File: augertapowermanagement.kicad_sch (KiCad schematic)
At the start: 27 parts, among them J1 Screw_Terminal_01x02, J10 Screw_Terminal_01x10, J11 Screw_Terminal_01x10, J12 gnd block, J2 76825-0002, J3 USB_A_Stacked, J4 USB_A_Stacked, J5 USB_A_Stacked, J6 USB_A_Stacked, J7 Screw_Terminal_01x08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

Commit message: update
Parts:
- removed Q1: IRF6623, Package_DirectFET:DirectFET_ST, symbol Transistor_FET:IRF6623
- added K2: J107F1CS203VDC.80, cit:Relay_J107F, symbol Relay:DIPxx-1Cxx-51x
- added R16: 10k, Resistor_SMD:R_1210_3225Metric_Pad1.30x2.65mm_HandSolder, symbol Device:R_US
- TP1, TP3, TP4, TP5: Purchase (none) -> JUST PAD
- U24: Purchase (none) -> IN LAB
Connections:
- net +BATT: now also K2.7
- net -BATT: now also R2.1, K2.6, R16.2; no longer SW1.3 (C)
- net at C2.1, J9.1 (Pin_1), J9.2 (Pin_2)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: now also SW1.2 (B), TP3.1; no longer R2.1
- net at JP1.1 (A), JP5.2 (B), K1.7: now also K2.14; no longer K1.8
- new net: K2.1, R16.1
- new net: K2.2, SW1.1 (A)
- new net: R2.2, SW1.3 (C)
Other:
- moved on the sheet: R2, SW1, TP3

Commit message: update
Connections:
- net at J11.1 (Pin_1): now also U2.38 (CLK); no longer U2.36 (SD1)
- net at J11.3 (Pin_3): now also U2.36 (SD1); no longer U2.38 (CLK)
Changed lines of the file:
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@@
+    (stroke (width 0) (type default) (color 0 0 0 0))
+  )
+  (wire (pts (xy 90.17 143.51) (xy 90.17 162.56))
     (stroke (width 0) (type default) (color 0 0 0 0))
   )
@@
     (stroke (width 0) (type default) (color 0 0 0 0))
   )
-  (wire (pts (xy 87.63 142.24) (xy 118.11 142.24))
-    (stroke (width 0) (type default) (color 0 0 0 0))
-  )
   (wire (pts (xy 76.2 71.12) (xy 113.03 71.12))
     (stroke (width 0) (type default) (color 0 0 0 0))
@@
     (stroke (width 0) (type default) (color 0 0 0 0))
   )
+  (wire (pts (xy 123.19 144.78) (xy 87.63 144.78))
+    (stroke (width 0) (type default) (color 0 0 0 0))
+  )
   (wire (pts (xy 118.11 92.71) (xy 121.92 92.71))
     (stroke (width 0) (type default) (color 0 0 0 0))
@@
     (stroke (width 0) (type default) (color 0 0 0 0))
   )
-  (wire (pts (xy 90.17 162.56) (xy 90.17 143.51))
-    (stroke (width 0) (type default) (color 0 0 0 0))
-  )
   (wire (pts (xy 72.39 162.56) (xy 72.39 118.11))
     (stroke (width 0) (type default) (color 0 0 0 0))
@@
     (stroke (width 0) (type default) (color 0 0 0 0))
   )
-  (wire (pts (xy 92.71 144.78) (xy 123.19 144.78))
-    (stroke (width 0) (type default) (color 0 0 0 0))
-  )
   (wire (pts (xy 177.8 106.68) (xy 176.53 106.68))
     (stroke (width 0) (type default) (color 0 0 0 0))
@@
     (stroke (width 0) (type default) (color 0 0 0 0))
   )
+  (wire (pts (xy 92.71 142.24) (xy 118.11 142.24))
+    (stroke (width 0) (type default) (color 0 0 0 0))
+  )
   (wire (pts (xy 248.92 50.8) (xy 251.46 50.8))
     (stroke (width 0) (type default) (color 0 0 0 0))
@@
     (stroke (width 0) (type default) (color 0 0 0 0))
   )
+  (wire (pts (xy 87.63 144.78) (xy 87.63 162.56))
+    (stroke (width 0) (type default) (color 0 0 0 0))
+  )
   (wire (pts (xy 77.47 130.81) (xy 40.64 130.81))
     (stroke (width 0) (type default) (color 0 0 0 0))
@@
     (stroke (width 0) (type default) (color 0 0 0 0))
   )
+  (wire (pts (xy 92.71 142.24) (xy 92.71 162.56))
+    (stroke (width 0) (type default) (color 0 0 0 0))
+  )
   (wire (pts (xy 201.93 96.52) (xy 266.7 96.52))
     (stroke (width 0) (type default) (color 0 0 0 0))
@@
     (stroke (width 0) (type default) (color 0 0 0 0))
   )
-  (wire (pts (xy 87.63 162.56) (xy 87.63 142.24))
-    (stroke (width 0) (type default) (color 0 0 0 0))
-  )
   (wire (pts (xy 180.34 50.8) (xy 180.34 45.72))
     (stroke (width 0) (type default) (color 0 0 0 0))
@@
     (stroke (width 0) (type default) (color 0 0 0 0))
   )
-  (wire (pts (xy 92.71 162.56) (xy 92.71 144.78))
-    (stroke (width 0) (type default) (color 0 0 0 0))
-  )

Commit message: update
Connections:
- net power_conversion/routerp: now also J7.1 (Pin_1)
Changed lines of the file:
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@@
   (junction (at 113.03 71.12) (diameter 0) (color 0 0 0 0)
   )
-  (junction (at 199.39 99.06) (diameter 0) (color 0 0 0 0)
+  (junction (at 175.26 93.98) (diameter 0) (color 0 0 0 0)
   )
   (junction (at 31.75 179.07) (diameter 0) (color 0 0 0 0)
@@
   (no_connect (at 190.5 144.78))
   (no_connect (at 190.5 147.32))
+  (wire (pts (xy 175.26 93.98) (xy 175.26 88.9))
+    (stroke (width 0) (type default) (color 0 0 0 0))
+  )
   (wire (pts (xy 118.11 107.95) (xy 139.7 107.95))
     (stroke (width 0) (type default) (color 0 0 0 0))
@@
     (stroke (width 0) (type default) (color 0 0 0 0))
   )
+  (wire (pts (xy 175.26 93.98) (xy 177.8 93.98))
+    (stroke (width 0) (type default) (color 0 0 0 0))
+  )
   (wire (pts (xy 199.39 55.88) (xy 199.39 58.42))
     (stroke (width 0) (type default) (color 0 0 0 0))
@@
     (stroke (width 0) (type default) (color 0 0 0 0))
   )
-  (wire (pts (xy 184.15 80.01) (xy 199.39 80.01))
+  (wire (pts (xy 184.15 81.28) (xy 199.39 81.28))
     (stroke (width 0) (type default) (color 0 0 0 0))
   )
@@
     (stroke (width 0) (type default) (color 0 0 0 0))
   )
-  (wire (pts (xy 187.96 127) (xy 187.96 82.55))
-    (stroke (width 0) (type default) (color 0 0 0 0))
-  )
   (wire (pts (xy 69.85 123.19) (xy 77.47 123.19))
     (stroke (width 0) (type default) (color 0 0 0 0))
@@
     (stroke (width 0) (type default) (color 0 0 0 0))
   )
+  (wire (pts (xy 187.96 82.55) (xy 187.96 127))
+    (stroke (width 0) (type default) (color 0 0 0 0))
+  )
   (wire (pts (xy 43.18 144.78) (xy 43.18 133.35))
     (stroke (width 0) (type default) (color 0 0 0 0))
@@
     (stroke (width 0) (type default) (color 0 0 0 0))
   )
+  (wire (pts (xy 199.39 81.28) (xy 199.39 99.06))
+    (stroke (width 0) (type default) (color 0 0 0 0))
+  )
   (wire (pts (xy 173.99 86.36) (xy 173.99 104.14))
     (stroke (width 0) (type default) (color 0 0 0 0))
@@
     (stroke (width 0) (type default) (color 0 0 0 0))
   )
-  (wire (pts (xy 146.05 93.98) (xy 177.8 93.98))
+  (wire (pts (xy 146.05 93.98) (xy 175.26 93.98))
     (stroke (width 0) (type default) (color 0 0 0 0))
   )
@@
     (stroke (width 0) (type default) (color 0 0 0 0))
   )
-  (wire (pts (xy 195.58 99.06) (xy 199.39 99.06))
+  (wire (pts (xy 175.26 88.9) (xy 177.8 88.9))
     (stroke (width 0) (type default) (color 0 0 0 0))
   )
@@
     (stroke (width 0) (type default) (color 0 0 0 0))
   )
+  (wire (pts (xy 184.15 80.01) (xy 184.15 81.28))
+    (stroke (width 0) (type default) (color 0 0 0 0))
+  )
   (wire (pts (xy 201.93 96.52) (xy 266.7 96.52))
     (stroke (width 0) (type default) (color 0 0 0 0))
@@
     (stroke (width 0) (type default) (color 0 0 0 0))
   )
-  (wire (pts (xy 199.39 80.01) (xy 199.39 99.06))
-    (stroke (width 0) (type default) (color 0 0 0 0))
-  )

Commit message: update
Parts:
- JP1, JP5: footprint Connector_PinHeader_2.00mm:PinHeader_1x02_P2.00mm_Horizontal -> cit:JUMPER_5102TR; Purchase NA, JUST pads -> https://www.digikey.com/en/products/detail/keystone-electro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
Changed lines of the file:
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@@
     (property "Reference" "JP1" (id 0) (at 100.33 29.21 0))
     (property "Value" "Jumper_2_Open" (id 1) (at 100.33 31.75 0))
-    (property "Footprint" "Connector_PinHeader_2.00mm:PinHeader_1x02_P2.00mm_Horizontal" (id 2) (at 100.33 35.56 0)
-      (effects (font (size 1.27 1.27)) hide)
-    )
-    (property "Datasheet" "~" (id 3) (at 100.33 35.56 0)
-      (effects (font (size 1.27 1.27)) hide)
-    )
-    (property "Purchase" "NA, JUST pads" (id 4) (at 100.33 35.56 0)
+    (property "Footprint" "cit:JUMPER_5102TR" (id 2) (at 100.33 35.56 0)
+      (effects (font (size 1.27 1.27)) hide)
+    )
+    (property "Datasheet" "https://www.digikey.com/en/products/detail/keystone-electronics/5102TR/4759688" (id 3) (at 100.33 35.56 0)
+      (effects (font (size 1.27 1.27)) hide)
+    )
+    (property "Purchase" "https://www.digikey.com/en/products/detail/keystone-electronics/5102TR/4759688" (id 4) (at 100.33 35.56 0)
       (effects (font (size 1.27 1.27)) hide)
     )
@@
     (property "Reference" "JP5" (id 0) (at 50.8 34.29 0))
     (property "Value" "Jumper_2_Open" (id 1) (at 60.96 36.83 0))
-    (property "Footprint" "Connector_PinHeader_2.00mm:PinHeader_1x02_P2.00mm_Horizontal" (id 2) (at 50.8 40.64 0)
-      (effects (font (size 1.27 1.27)) hide)
-    )
-    (property "Datasheet" "~" (id 3) (at 50.8 40.64 0)
-      (effects (font (size 1.27 1.27)) hide)
-    )
-    (property "Purchase" "NA, JUST pads" (id 4) (at 50.8 40.64 0)
+    (property "Footprint" "cit:JUMPER_5102TR" (id 2) (at 50.8 40.64 0)
+      (effects (font (size 1.27 1.27)) hide)
+    )
+    (property "Datasheet" "https://www.digikey.com/en/products/detail/keystone-electronics/5102TR/4759688" (id 3) (at 50.8 40.64 0)
+      (effects (font (size 1.27 1.27)) hide)
+    )
+    (property "Purchase" "https://www.digikey.com/en/products/detail/keystone-electronics/5102TR/4759688" (id 4) (at 50.8 40.64 0)
       (effects (font (size 1.27 1.27)) hide)
     )
@@
     )
     (path "/74a29476-3c13-4143-84d6-566dfae4024a"
-      (reference "JP1") (unit 1) (value "Jumper_2_Open") (footprint "Connector_PinHeader_2.00mm:PinHeader_1x02_P2.00mm_Horizontal")
+      (reference "JP1") (unit 1) (value "Jumper_2_Open") (footprint "cit:JUMPER_5102TR")
     )
     (path "/8a8c373f-9bc3-4cf7-8f41-4802da916698/50a4d4a6-86ed-460b-979f-ababc72cae1c"
-      (reference "JP2") (unit 1) (value "Jumper_2_Open") (footprint "Connector_PinHeader_2.00mm:PinHeader_1x02_P2.00mm_Horizontal")
+      (reference "JP2") (unit 1) (value "Jumper_2_Open") (footprint "cit:JUMPER_5102TR")
     )
     (path "/8a8c373f-9bc3-4cf7-8f41-4802da916698/5768f29d-5de4-4595-abf0-f6083c155be3"
@@
     )
     (path "/94034c37-7b26-417f-a611-c68fda56c0c1"
-      (reference "JP5") (unit 1) (value "Jumper_2_Open") (footprint "Connector_PinHeader_2.00mm:PinHeader_1x02_P2.00mm_Horizontal")
+      (reference "JP5") (unit 1) (value "Jumper_2_Open") (footprint "cit:JUMPER_5102TR")
     )
     (path "/8a8c373f-9bc3-4cf7-8f41-4802da916698/1ed5a3a3-3988-44f5-970d-7e971f9abf8f"
-      (reference "JP6") (unit 1) (value "Jumper_2_Open") (footprint "Connector_PinHeader_2.00mm:PinHeader_1x02_P2.00mm_Horizontal")
+      (reference "JP6") (unit 1) (value "Jumper_2_Open") (footprint "cit:JUMPER_5102TR")
     )
     (path "/1347a48f-a9f7-470c-893f-af03f52f8d81"

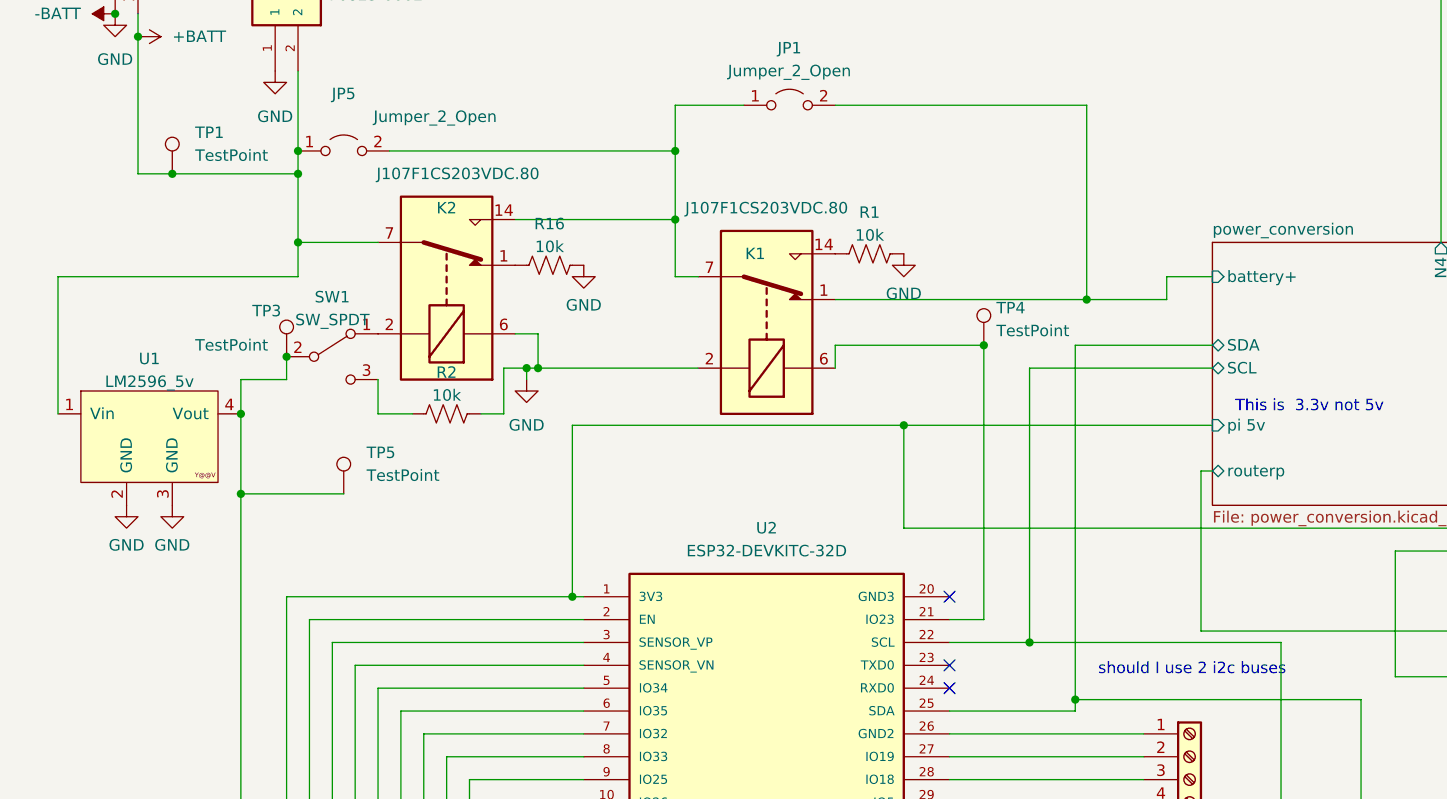
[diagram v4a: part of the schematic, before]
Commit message: Improved power plane, relay changes, i2c resistor changes
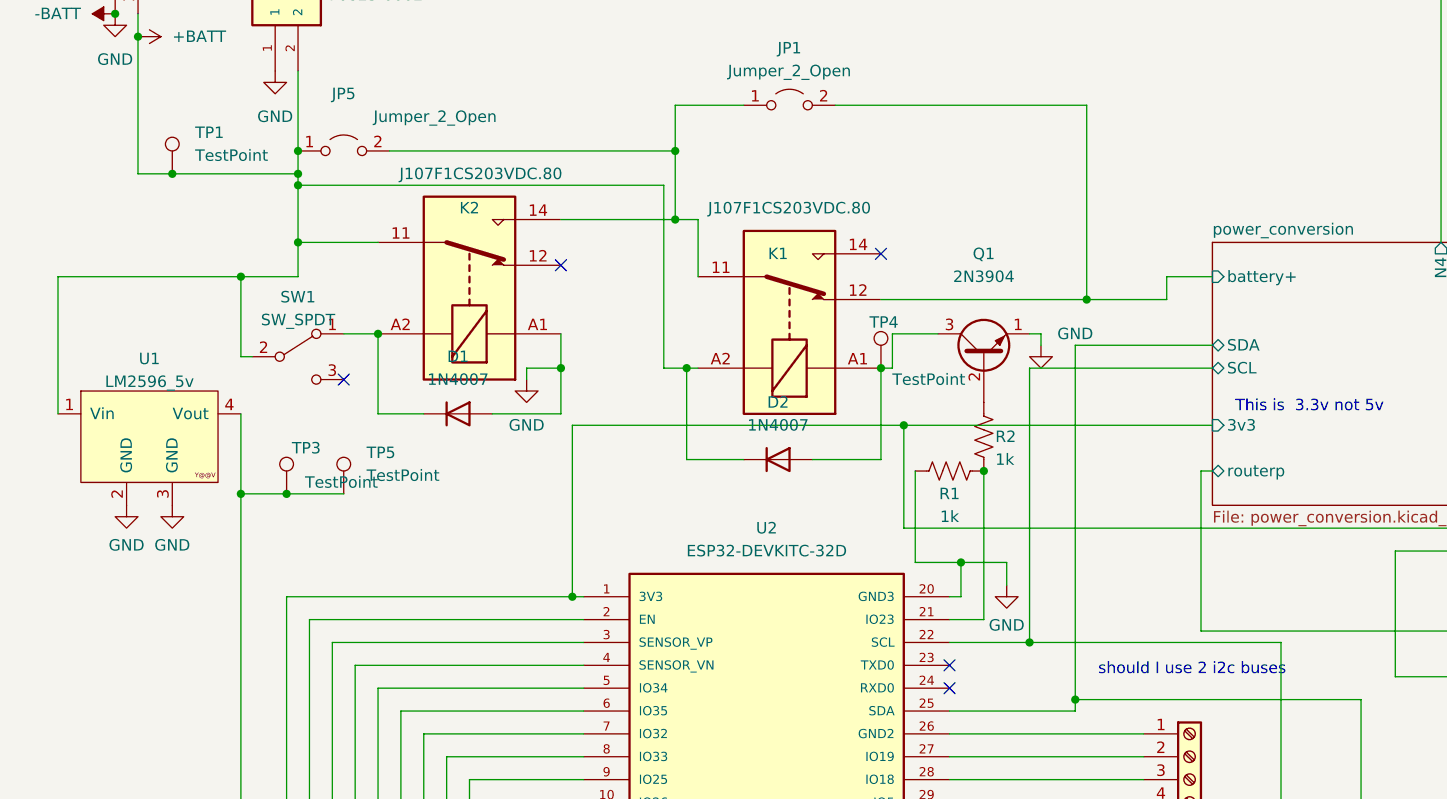
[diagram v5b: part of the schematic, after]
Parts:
- removed R16: 10k, Resistor_SMD:R_1210_3225Metric_Pad1.30x2.65mm_HandSolder, symbol Device:R_US
- added D1, D2: 1N4007, Diode_THT:D_DO-41_SOD81_P10.16mm_Horizontal, symbol Diode:1N4007
- added Q1: 2N3904, Package_TO_SOT_THT:TO-92_HandSolder, symbol Transistor_BJT:2N3904
- K1, K2: footprint cit:Relay_J107F -> Relay_THT:Relay_SPDT_RAYEX-L90S; symbol Relay:DIPxx-1Cxx-51x -> Relay:RAYEX-L90S
- R1, R2: value 10k -> 1k; footprint Resistor_SMD:R_1210_3225Metric_Pad1.30x2.65mm_HandSolder -> Resistor_SMD:R_1206_3216Metric_Pad1.30x1.75mm_HandSolder; Purchase https://www.digikey.com/en/products/detail/vishay-dale/CRCW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 -> (none)
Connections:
- net +BATT: now also K1.A2, K2.11, SW1.2 (B), D2.1 (K); no longer K2.7
- net -BATT: now also K2.A1, R1.1, U2.20 (GND3), D1.2 (A), Q1.1 (E); no longer K1.2, K2.6, R1.2, R2.1
- net power_conversion/battery+: now also K1.12; no longer K1.1
- net at JP1.1 (A), JP5.2 (B), K2.14: now also K1.11; no longer K1.7
- net at SW1.1 (A): now also K2.A2, D1.1 (K); no longer K2.2
- net at C2.1, J9.1 (Pin_1), J9.2 (Pin_2)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: no longer SW1.2 (B)
- net at K1.14: no longer R1.1
- net at R2.2: now also Q1.2 (B); no longer SW1.3 (C)
- net power_conversion/pi 5v renamed power_conversion/3v3
- new net: R1.2, R2.1, U2.21 (IO23)
- new net: D2.2 (A), K1.A1, Q1.3 (C), TP4.1
- no-connect marks 23 -> 25
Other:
- sheet power_conversion ports: added 3v3; removed pi 5v
- moved on the sheet: SW1, TP3, TP4
